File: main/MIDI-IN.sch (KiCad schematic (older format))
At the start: 5 parts

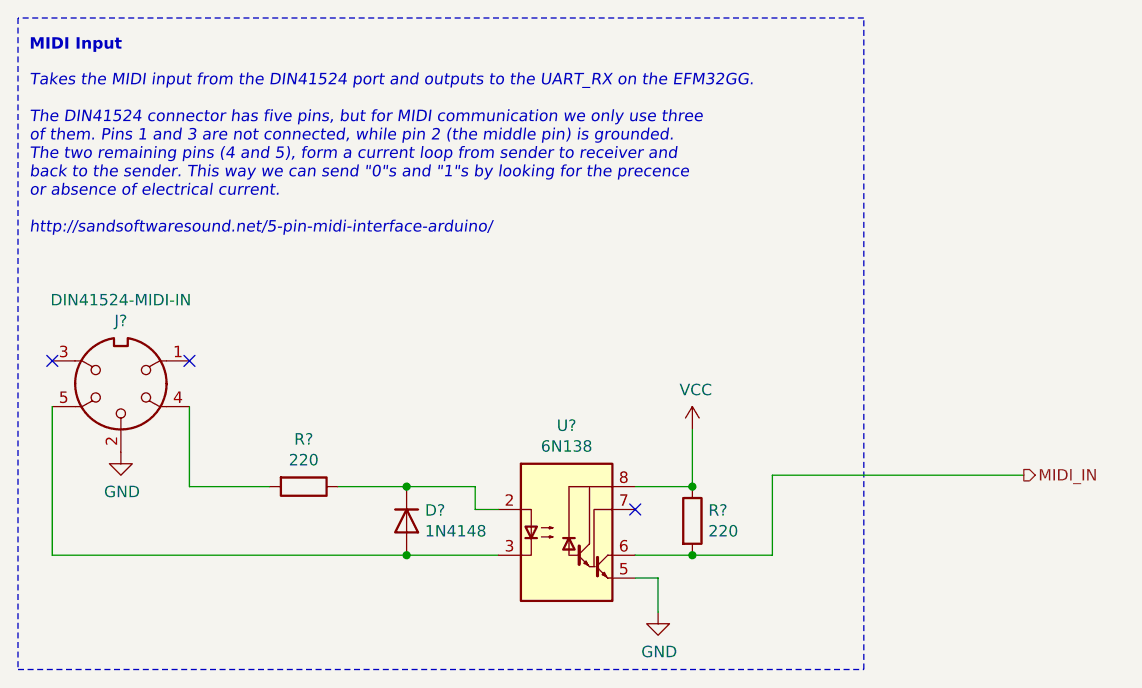
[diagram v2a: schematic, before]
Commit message: Setup DAC.
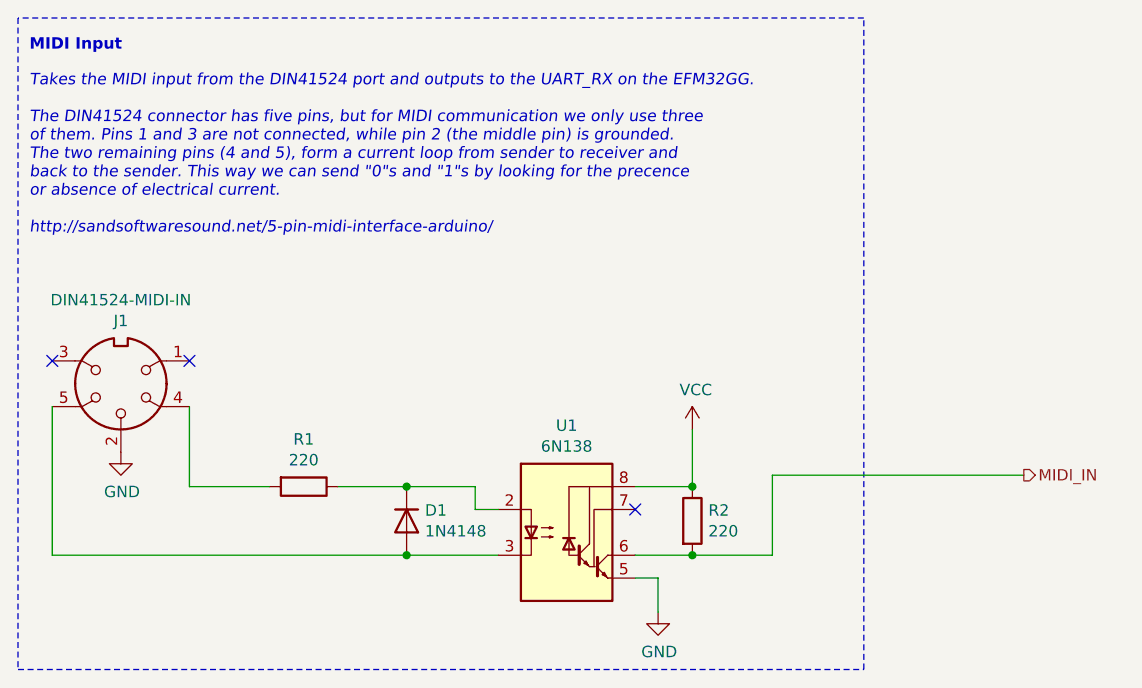
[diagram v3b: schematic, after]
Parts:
- gave numbers to parts that had none: 5
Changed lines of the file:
@@
 $Descr A4 11693 8268
 encoding utf-8
-Sheet 3 4
+Sheet 2 5
 Title ""
 Date ""
@@
 $EndDescr
 $Comp
-L MIDI:DIN41524-MIDI-IN J?
+L MIDI:DIN41524-MIDI-IN J1
 U 1 1 61403606
 P 4400 4000
-F 0 "J?" H 4400 3725 50  0000 C CNN
+F 0 "J1" H 4400 3725 50  0000 C CNN
 F 1 "DIN41524-MIDI-IN" H 4400 3634 50  0000 C CNN
 F 2 "" H 4400 4000 50  0001 C CNN
@@
 	3950 5250 7650 5250
 $Comp
-L power:GND #PWR?
+L power:GND #PWR01
 U 1 1 61403610
 P 4400 4300
-F 0 "#PWR?" H 4400 4050 50  0001 C CNN
+F 0 "#PWR01" H 4400 4050 50  0001 C CNN
 F 1 "GND" H 4405 4127 50  0000 C CNN
 F 2 "" H 4400 4300 50  0001 C CNN
@@
 $EndComp
 $Comp
-L Diode:1N4148 D?
+L Diode:1N4148 D1
 U 1 1 61403616
 P 5650 4600
-F 0 "D?" V 5604 4680 50  0000 L CNN
+F 0 "D1" V 5604 4680 50  0000 L CNN
 F 1 "1N4148" V 5695 4680 50  0000 L CNN
 F 2 "Diode_THT:D_DO-35_SOD27_P7.62mm_Horizontal" H 5650 4425 50  0001 C CNN
@@
 $EndComp
 $Comp
-L Device:R R?
+L Device:R R1
 U 1 1 6140361C
 P 5200 4450
-F 0 "R?" V 4993 4450 50  0000 C CNN
+F 0 "R1" V 4993 4450 50  0000 C CNN
 F 1 "220" V 5084 4450 50  0000 C CNN
 F 2 "" V 5130 4450 50  0001 C CNN
@@
 	5350 4450 5650 4450
 $Comp
-L Isolator:6N138 U?
+L Isolator:6N138 U1
 U 1 1 61403627
 P 6350 4650
-F 0 "U?" H 6350 5117 50  0000 C CNN
+F 0 "U1" H 6350 5117 50  0000 C CNN
 F 1 "6N138" H 6350 5026 50  0000 C CNN
 F 2 "" H 6640 4350 50  0001 C CNN
@@
 Connection ~ 5650 4450
 $Comp
-L power:GND #PWR?
+L power:GND #PWR02
 U 1 1 61403633
 P 6750 5000
-F 0 "#PWR?" H 6750 4750 50  0001 C CNN
+F 0 "#PWR02" H 6750 4750 50  0001 C CNN
 F 1 "GND" H 6755 4827 50  0000 C CNN
 F 2 "" H 6750 5000 50  0001 C CNN
@@
 	6650 4750 6900 4750
 $Comp
-L Device:R R?
+L Device:R R2
 U 1 1 6140363C
 P 6900 4600
-F 0 "R?" H 6970 4646 50  0000 L CNN
+F 0 "R2" H 6970 4646 50  0000 L CNN
 F 1 "220" H 6970 4555 50  0000 L CNN
 F 2 "" V 6830 4600 50  0001 C CNN
@@
 	6650 4450 6900 4450
 $Comp
-L power:VCC #PWR?
+L power:VCC #PWR03
 U 1 1 61403643
 P 6900 4200
-F 0 "#PWR?" H 6900 4050 50  0001 C CNN
+F 0 "#PWR03" H 6900 4050 50  0001 C CNN
 F 1 "VCC" H 6915 4373 50  0000 C CNN
 F 2 "" H 6900 4200 50  0001 C CNN

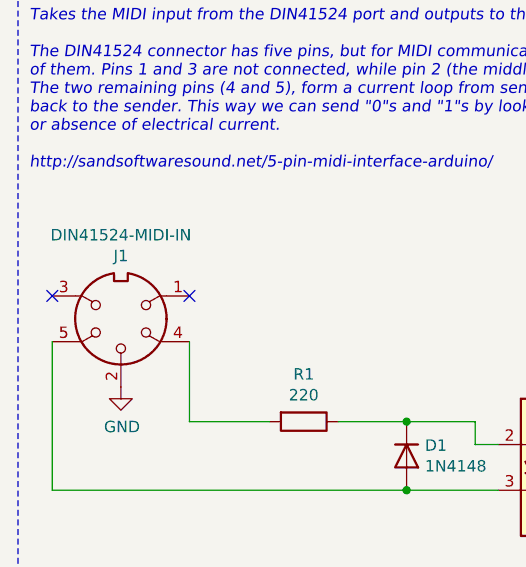
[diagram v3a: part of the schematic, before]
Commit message: Used wrong MIDI connector
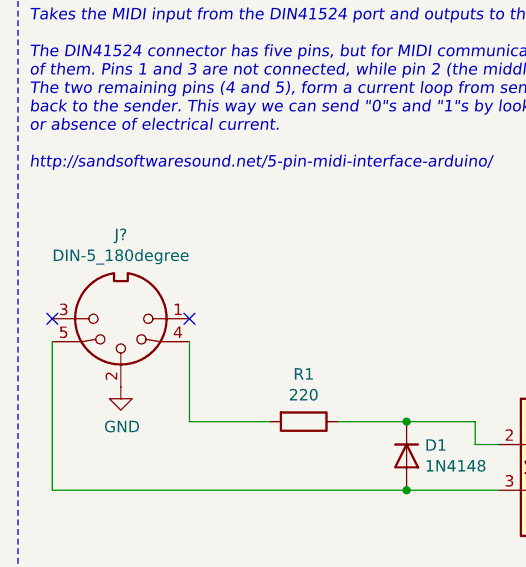
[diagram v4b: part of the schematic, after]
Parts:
- removed J1: DIN41524-MIDI-IN, symbol MIDI:DIN41524-MIDI-IN
- added J?: DIN-5_180degree, symbol Connector:DIN-5_180degree
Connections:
- net GND: now also J?.2
- net at R1.2: now also J?.4
- net at D1.2 (A), U1.3 (C2): now also J?.5
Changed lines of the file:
@@
 Comment4 ""
 $EndDescr
-$Comp
-L MIDI:DIN41524-MIDI-IN J1
-U 1 1 61403606
-P 4400 4000
-F 0 "J1" H 4400 3725 50  0000 C CNN
-F 1 "DIN41524-MIDI-IN" H 4400 3634 50  0000 C CNN
-F 2 "" H 4400 4000 50  0001 C CNN
-F 3 "http://www.mouser.com/ds/2/18/40_c091_abd_e-75918.pdf" H 4400 4000 50  0001 C CNN
-	1    4400 4000
-	-1   0    0    1
-$EndComp
-NoConn ~ 4100 3900
-NoConn ~ 4700 3900
+NoConn ~ 4100 4000
+NoConn ~ 4700 4000
 Wire Notes Line
 	3950 2400 3950 5250
@@
 Text HLabel 8350 4400 2    50   Output ~ 0
 MIDI_IN
+$Comp
+L Connector:DIN-5_180degree J?
+U 1 1 6146F928
+P 4400 4000
+F 0 "J?" H 4400 3633 50  0000 C CNN
+F 1 "DIN-5_180degree" H 4400 3724 50  0000 C CNN
+F 2 "" H 4400 4000 50  0001 C CNN
+F 3 "http://www.mouser.com/ds/2/18/40_c091_abd_e-75918.pdf" H 4400 4000 50  0001 C CNN
+	1    4400 4000
+	-1   0    0    1
+$EndComp
 $EndSCHEMATC

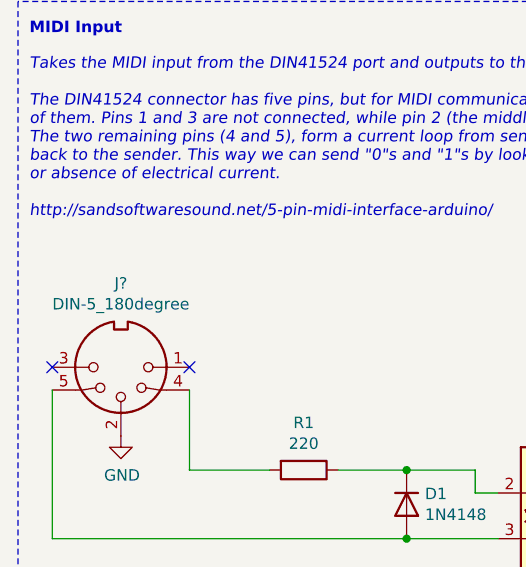
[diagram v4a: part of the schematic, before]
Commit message: Add DAC footprint
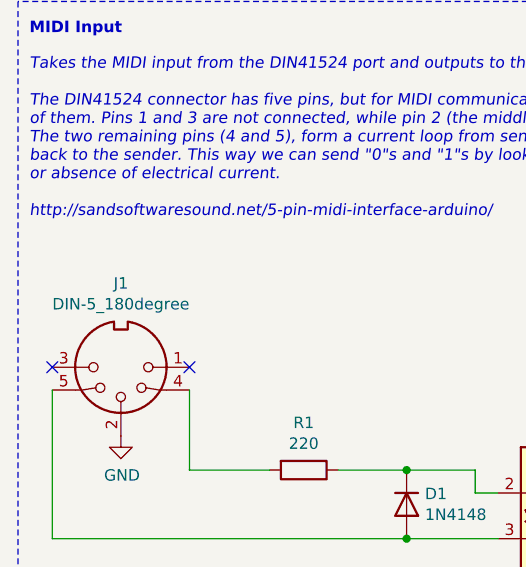
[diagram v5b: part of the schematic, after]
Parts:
- gave numbers to parts that had none: 1
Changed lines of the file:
@@
 MIDI_IN
 $Comp
-L Connector:DIN-5_180degree J?
+L Connector:DIN-5_180degree J1
 U 1 1 6146F928
 P 4400 4000
-F 0 "J?" H 4400 3633 50  0000 C CNN
+F 0 "J1" H 4400 3633 50  0000 C CNN
 F 1 "DIN-5_180degree" H 4400 3724 50  0000 C CNN
 F 2 "" H 4400 4000 50  0001 C CNN

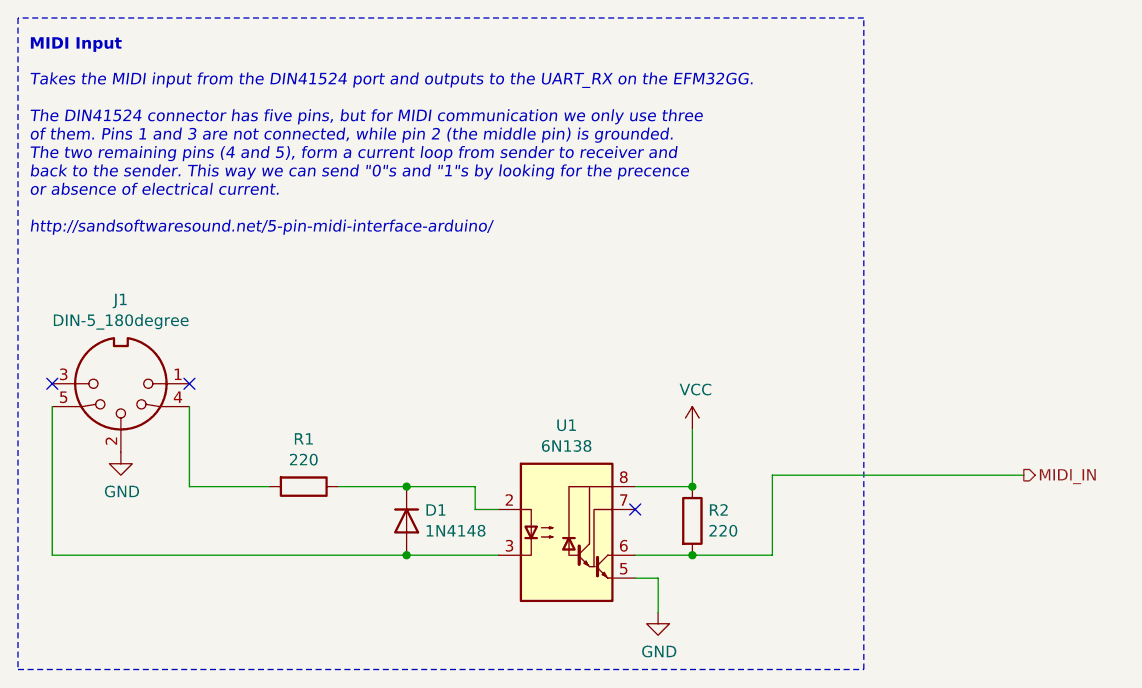
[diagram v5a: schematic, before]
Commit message: Setup FPGA power connections, connect FPGA flash
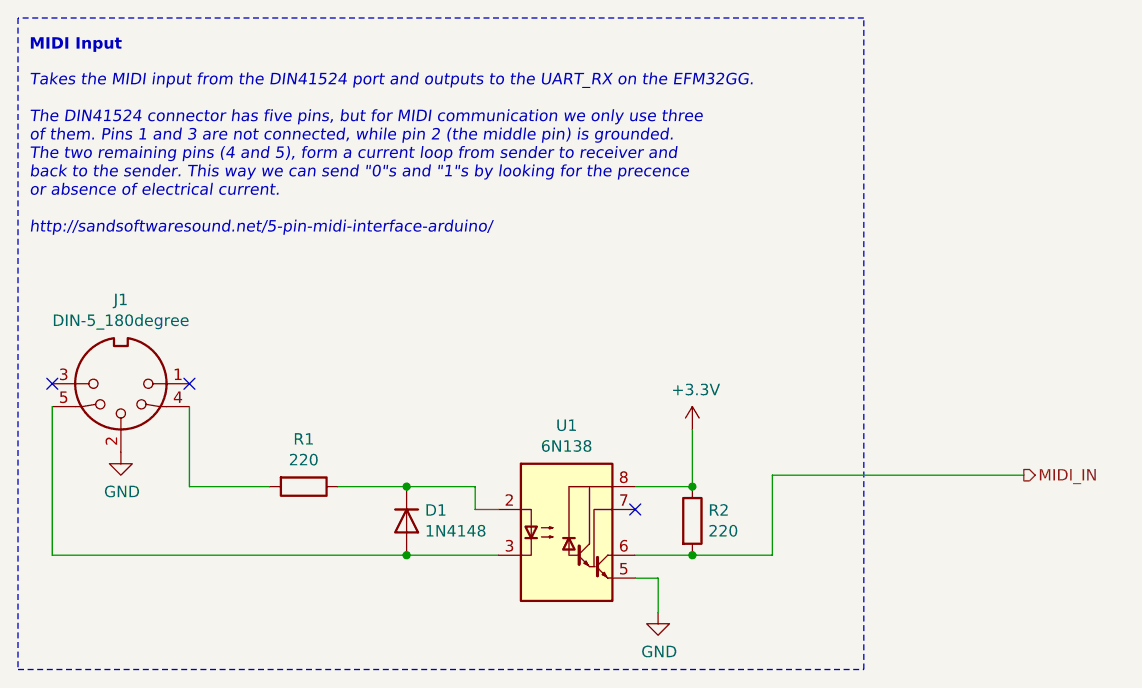
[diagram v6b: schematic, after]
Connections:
- net VCC renamed +3V3
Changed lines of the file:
@@
 $Descr A4 11693 8268
 encoding utf-8
-Sheet 2 5
+Sheet 2 6
 Title ""
 Date ""
@@
 Wire Wire Line
 	6650 4450 6900 4450
-$Comp
-L power:VCC #PWR03
-U 1 1 61403643
-P 6900 4200
-F 0 "#PWR03" H 6900 4050 50  0001 C CNN
-F 1 "VCC" H 6915 4373 50  0000 C CNN
-F 2 "" H 6900 4200 50  0001 C CNN
-F 3 "" H 6900 4200 50  0001 C CNN
-	1    6900 4200
-	1    0    0    -1
-$EndComp
 Wire Wire Line
 	6900 4450 6900 4200
@@
 	-1   0    0    1
 $EndComp
+$Comp
+L power:+3.3V #PWR?
+U 1 1 6148E544
+P 6900 4200
+F 0 "#PWR?" H 6900 4050 50  0001 C CNN
+F 1 "+3.3V" H 6915 4373 50  0000 C CNN
+F 2 "" H 6900 4200 50  0001 C CNN
+F 3 "" H 6900 4200 50  0001 C CNN
+	1    6900 4200
+	1    0    0    -1
+$EndComp
 $EndSCHEMATC
